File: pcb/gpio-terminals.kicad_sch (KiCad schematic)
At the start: 3 parts, among them J2 Screw_Terminal_01x02, J3 Screw_Terminal_01x03, J4 JST-PH-4

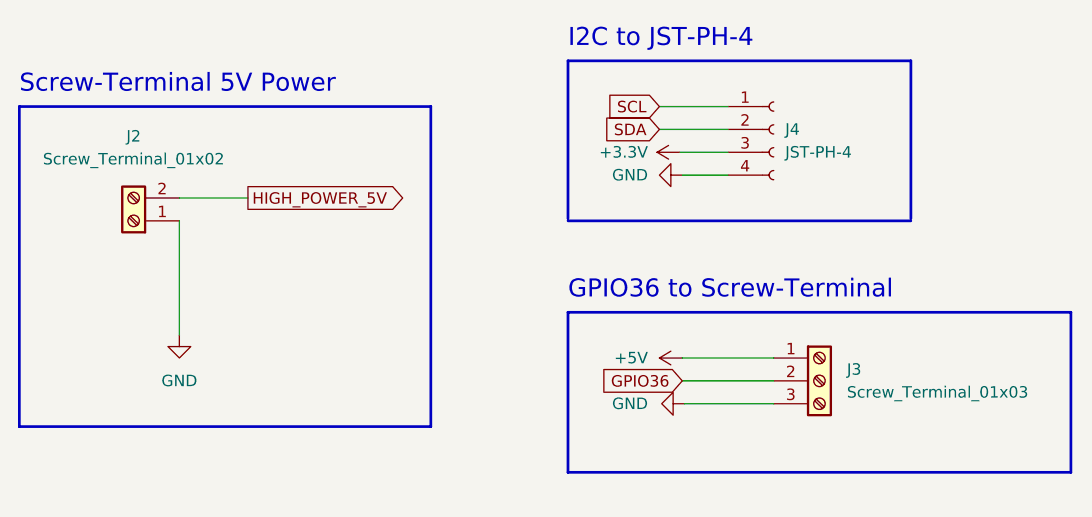
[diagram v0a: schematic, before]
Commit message: REF PCB Layout, Switch to new USB-C Receptable
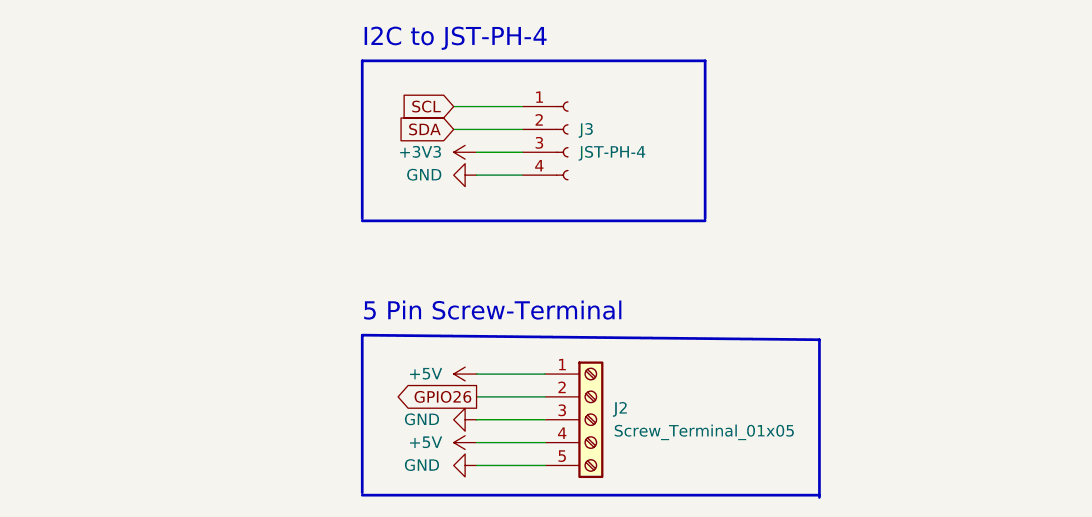
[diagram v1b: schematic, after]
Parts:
- removed J2: Screw_Terminal_01x02, TerminalBlock_Phoenix:TerminalBlock_Phoenix_MKDS-1,5-2-5.08_1x02_P5.08mm_Horizontal, symbol Connector:Screw_Terminal_01x02
- removed J3: Screw_Terminal_01x03, TerminalBlock_Phoenix:TerminalBlock_Phoenix_MKDS-1,5-3-5.08_1x03_P5.08mm_Horizontal, symbol Connector:Screw_Terminal_01x03
- added J2: Screw_Terminal_01x05, TerminalBlock_Phoenix:TerminalBlock_Phoenix_MKDS-1,5-5-5.08_1x05_P5.08mm_Horizontal, symbol Connector:Screw_Terminal_01x05
- renumbered J4 to J3
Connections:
- net +5V: now also J2.1 (Pin_1), J2.4 (Pin_4)
- net GND: now also J2.3 (Pin_3), J2.5 (Pin_5)
- new net GPIO26: J2.2 (Pin_2)
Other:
- note added: "5 Pin Screw-Terminal"
- note removed: "GPIO36 to Screw-Terminal"
- note removed: "Screw-Terminal 5V Power"
- moved on the sheet: J3
